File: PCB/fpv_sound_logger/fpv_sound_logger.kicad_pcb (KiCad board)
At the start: 2 copper layers, 32.1 x 25.8 mm, 47 parts, among them CN1 SM04B-SRSS-TB(LF)(SN), IC1 W25Q128JVSIQ, IC2 NCP1117ST33T3G, J1 DM3D-SF, U1 RP2040, U2 INMP441ACEZ-R7, Y1 ABM8-272-T3

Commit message: PCB: started routing
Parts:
- C1, C14, C16, C17, C18, C2, C3, D2, R4, R5, R6: moved to B.Cu
- IC2: moved to F.Cu
- moved TP1 45.7 mm to (152.8, 94.5)
- moved TP3 44.4 mm to (152.7, 96.7)
- moved TP2 42.5 mm to (150.5, 94.5)
- moved TP4 41.5 mm to (150.5, 96.7)
- moved R3 37.8 mm to (150.7, 85.9), turned to 180 degrees
- moved C16 36.4 mm to (138.8, 97.2), turned to -90 degrees
- moved R9 36.1 mm to (148.7, 96.7), turned to -90 degrees
- moved C12 35.6 mm to (151.8, 92.3)
- moved C15 35.2 mm to (149.2, 99.4)
- moved R7 35.1 mm to (147.5, 93.0)
- moved R10 33.9 mm to (146.7, 98.0)
- moved R11 33.5 mm to (146.6, 99.0)
- moved R8 33.3 mm to (148.7, 85.9), turned to 180 degrees
- moved R4 32.6 mm to (143.0, 96.4)
- moved C13 29.3 mm to (152.5, 85.5), turned to 90 degrees
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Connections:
- net Net-(U1-USB_DM) renamed /USB_DIFF-
- net Net-(U1-USB_DP) renamed /USB_DIFF+
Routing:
- net /GPIO2: track 0.00 -> 19.1 mm
- net VBUS: track 0.00 -> 19.1 mm, vias 0 -> 3
- net /GPIO1: track 0.00 -> 17.3 mm
- net /USB_D+: track 0.00 -> 12.7 mm
- net /USB_D-: track 0.00 -> 12.7 mm
- net +3V3: track 0.00 -> 10.3 mm, vias 0 -> 1
- net Net-(D1-A): track 0.00 -> 9.15 mm
- net /GPIO13: track 0.00 -> 7.87 mm, vias 0 -> 1
- net Net-(D2-K): track 0.00 -> 3.92 mm, vias 0 -> 1
- net GND: track 0.00 -> 3.85 mm
- net /USB_DIFF-: track 0.00 -> 2.15 mm
- net /USB_DIFF+: track 0.00 -> 2.15 mm
- net Net-(USB1-CC1): track 0.00 -> 1.45 mm, vias 0 -> 1
- added copper zone on F.Cu, net GND
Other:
- board size 32.1 x 25.8 mm -> 30.2 x 21.7 mm

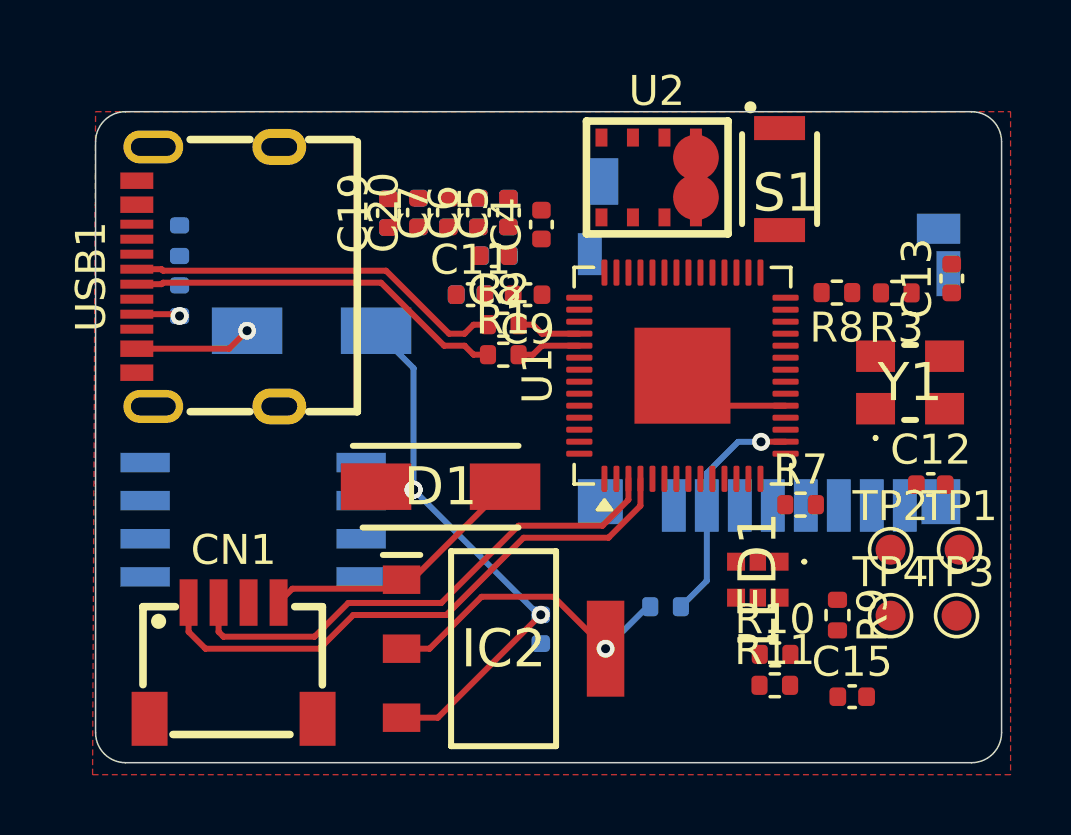
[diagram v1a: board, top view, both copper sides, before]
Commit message: PCB: finised routing - Changed clearance from 0.2 to 0.15 in the net class settings. - Increased track width from 0.3 to 0.4 for improved signal integrity. - Added a new net class for POWER with pattern GND. - Adjusted positions of GPIO labels for better alignment in the schematic:   - Moved GPIO3 from (119.38, 160.02) to (119.38, 165.1).   - Moved GPIO5 from (119.38, 165.1) to (119.38, 160.02).   - Moved GPIO10 from (129.54, 127) to (138.43, 121.92).   - Moved GPIO11 from (138.43, 121.92) to (129.54, 127).
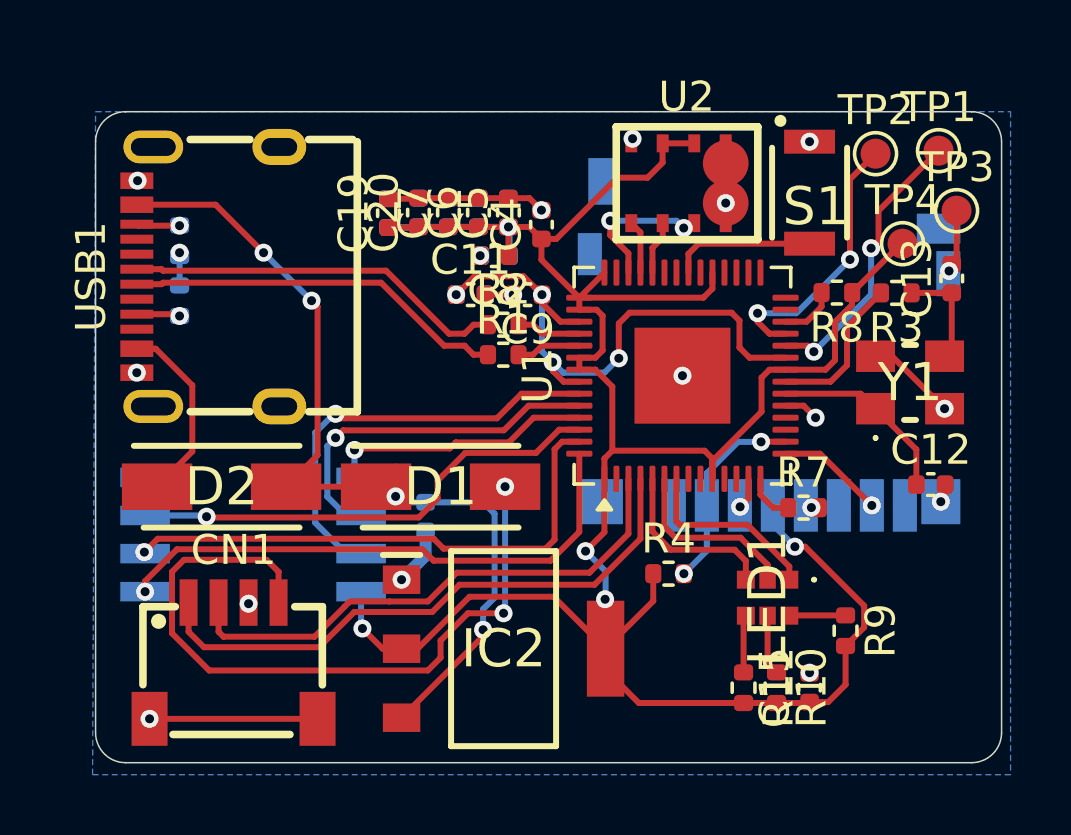
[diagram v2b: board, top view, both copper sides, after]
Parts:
- D2, R4: moved to F.Cu
- moved TP3 13.5 mm to (152.7, 83.2)
- moved TP1 13.3 mm to (152.1, 81.2)
- moved TP2 13.2 mm to (150.0, 81.3)
- moved TP4 12.4 mm to (150.9, 84.3)
- moved D2 6.00 mm to (128.2, 92.4)
- moved C16 5.37 mm to (135.0, 93.4)
- moved C15 1.45 mm to (147.8, 99.1), turned to 90 degrees
- moved R10 1.11 mm to (146.7, 99.1), turned to -90 degrees
- moved R4 1.10 mm to (143.1, 95.3)
- moved S1 1.10 mm to (147.8, 82.6)
- moved R11 1.04 mm to (145.6, 99.1), turned to -90 degrees
- moved U2 1.01 mm to (143.4, 82.3)
- moved LED1 0.68 mm to (146.4, 96.1)
- moved R9 0.59 mm to (149.0, 97.2)
- moved IC1 0.50 mm to (129.2, 94.0)
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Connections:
- J1 pad 3: /GPIO11 -> /GPIO10
- LED1 pad 1: /GPIO3 -> /GPIO5
- LED1 pad 3: /GPIO5 -> /GPIO3
- R7 pad 1: /GPIO10 -> /GPIO11
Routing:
- net +3V3: track 10.3 -> 88.2 mm, vias 1 -> 5
- net GND: track 3.85 -> 24.6 mm, vias 0 -> 18
- net +1V1: track 0.00 -> 19.6 mm, vias 0 -> 4
- net /QSPI_SS: track 0.00 -> 18.4 mm, vias 0 -> 1
- net /QSPI_SD1: track 0.00 -> 18.1 mm, vias 0 -> 1
- net /QSPI_SD2: track 0.00 -> 16.1 mm, vias 0 -> 1
- net Net-(D1-A): track 9.15 -> 23.9 mm, vias 0 -> 2
- net /QSPI_SD3: track 0.00 -> 14.4 mm, vias 0 -> 1
- net /QSPI_SCLK: track 0.00 -> 12.0 mm, vias 0 -> 1
- net VBUS: track 19.1 -> 29.7 mm, vias 3 -> 4
- net /SWCLK: track 0.00 -> 9.45 mm, vias 0 -> 2
- net /SWD: track 0.00 -> 9.09 mm, vias 0 -> 2
- net /QSPI_SD0: track 0.00 -> 9.01 mm, vias 0 -> 1
- net /XIN: track 0.00 -> 6.30 mm
- net /GPIO5: track 0.00 -> 6.25 mm
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- added copper zone on B.Cu, net GND
- removed copper zone on F.Cu, net GND

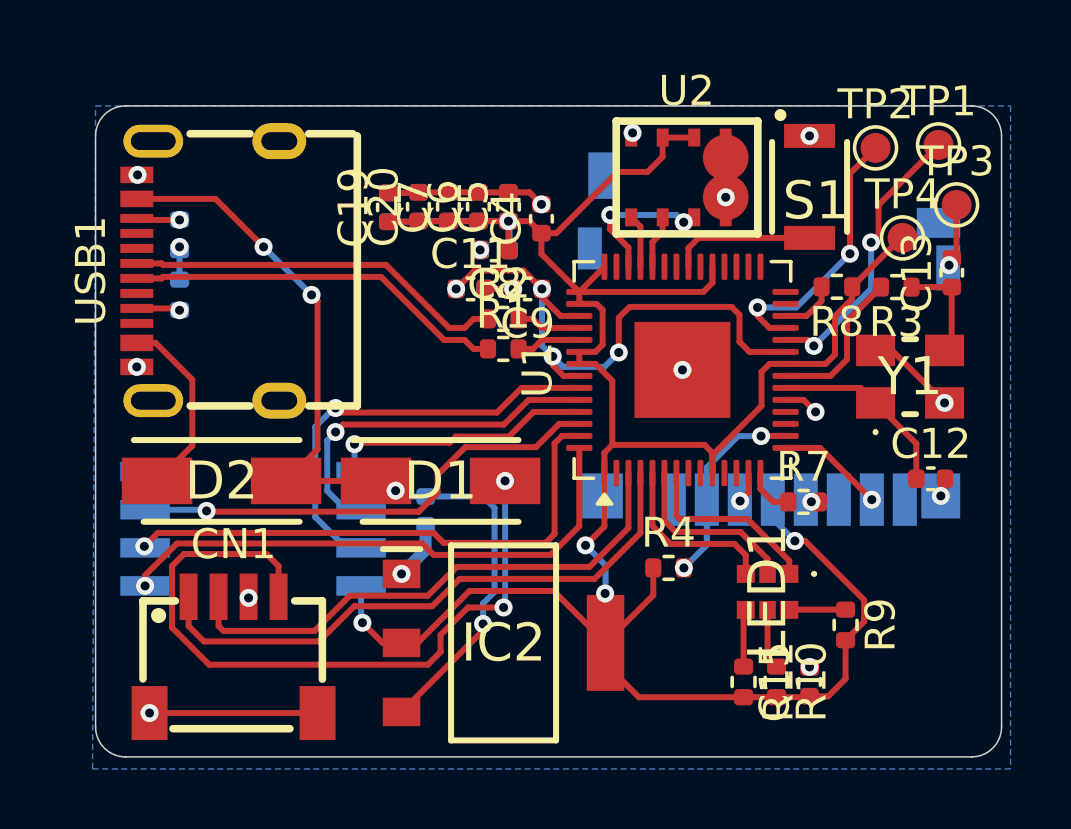
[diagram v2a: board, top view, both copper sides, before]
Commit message: PCB: finishes on board design - DRC check - Placed text - add 3d files for 3d viewer
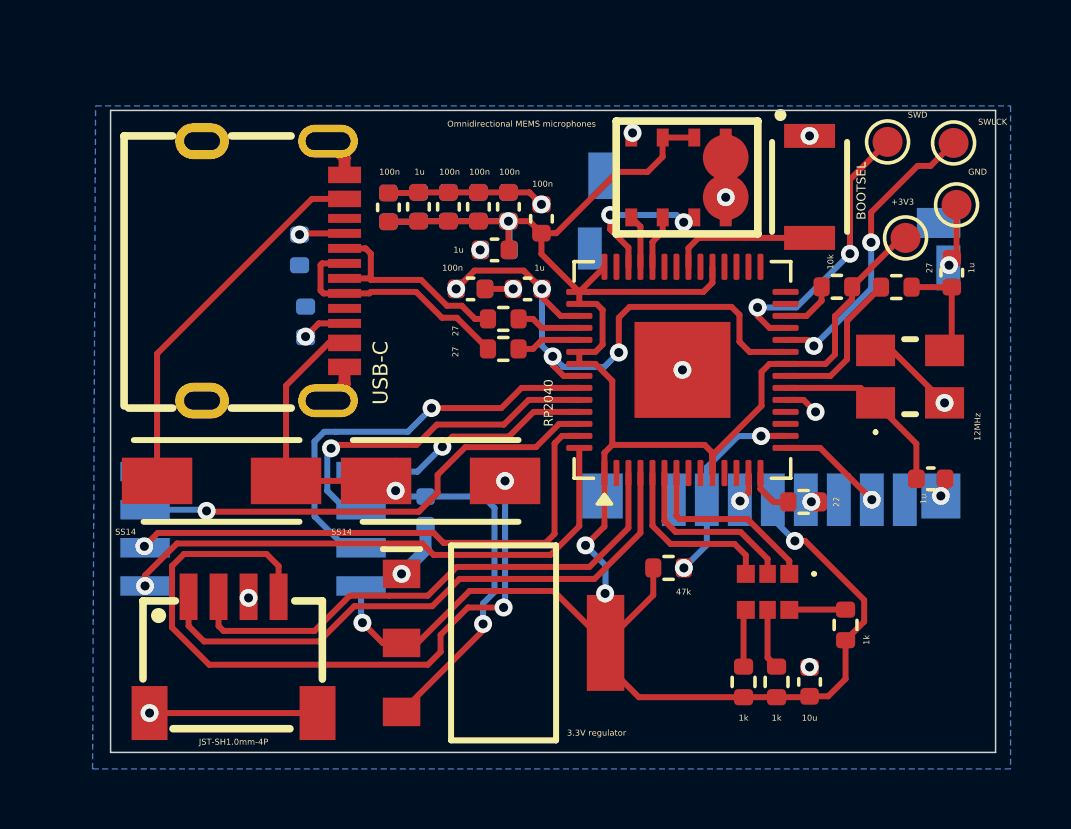
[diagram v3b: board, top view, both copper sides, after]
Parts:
- 3.3V regulator: renamed from IC2
- Flash memory: renamed from IC1
- Omnidirectional MEMS microphones: renamed from U2
- microSD card: renamed from J1
- moved 5k1 5.10 mm to (131.0, 87.1), turned to 90 degrees
- moved 5k1 4.27 mm to (130.8, 84.7), turned to -90 degrees
- moved USB-C 2.18 mm to (129.9, 85.4), turned to -90 degrees
- moved SWLCK 0.50 mm to (152.6, 81.1)
- moved SWD 0.45 mm to (150.4, 81.1)
- moved +3V3 0.10 mm to (151.0, 84.3)
- renumbered TP4 to +3V3, C19 to 100n, C1 to 100n, C18 to 100n, C7 to 100n, C11 to 100n, C6 to 100n, C5 to 100n, C4 to 100n, C3 to 100n, C10 to 100n, C2 to 100n, R8 to 10k, C15 to 10u, C16 to 10u, C17 to 10u, Y1 to 12MHz, R10 to 1k, R9 to 1k, R11 to 1k, C8 to 1u, C13 to 1u, C12 to 1u, C9 to 1u, C20 to 1u, C14 to 1u, R7 to 22, R3 to 27, R2 to 27, R1 to 27, R4 to 47k, R5 to 5k1, R6 to 5k1, TP3 to GND, CN1 to JST-SH1.0mm-4P, U1 to RP2040, D1 to SS14, D2 to SS14, TP2 to SWD, TP1 to SWLCK, USB1 to USB-C
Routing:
- net VBUS: track 29.7 -> 21.5 mm, vias 4 -> 2
- net Net-(D2-K): track 6.22 -> 12.6 mm
- net /USB_D-: track 12.7 -> 7.16 mm
- net /USB_D+: track 12.7 -> 8.10 mm
- net GND: track 24.6 -> 26.5 mm, vias 18 -> 15
- net /QSPI_SD0: track 9.01 -> 8.48 mm
- net /SWCLK: track 9.45 -> 9.97 mm
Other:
- board size 30.2 x 21.7 mm -> 29.5 x 21.4 mm
- board text added: "BOOTSEL"

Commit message: Refactor code structure and remove redundant sections for improved readability and maintainability
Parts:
- removed +3V3, GND, SWD, SWLCK: TestPoint, TestPoint:TestPoint_Pad_D1.0mm
- removed 100n (x11): 100n, Capacitor_SMD:C_0402_1005Metric
- removed 10k: 10k, Resistor_SMD:R_0402_1005Metric
- removed 10u (x3): 10u, Capacitor_SMD:C_0402_1005Metric
- removed 12MHz: ABM8-272-T3, fpv_sound_logger:ABM8272T3
- removed 1k (x3): 1k, Resistor_SMD:R_0402_1005Metric
- removed 1u (x6): 1u, Capacitor_SMD:C_0402_1005Metric
- removed 22: 22, Resistor_SMD:R_0402_1005Metric
- removed 27 (x3): 27, Resistor_SMD:R_0402_1005Metric
- removed 3.3V regulator: NCP1117ST33T3G, fpv_sound_logger:SOT230P700X180-4N
- removed 47k: 47k, Resistor_SMD:R_0402_1005Metric
- removed 5k1 (x2): 5k1, Resistor_SMD:R_0402_1005Metric
- removed Flash memory: W25Q128JVSIQ, fpv_sound_logger:SOIC127P790X216-8N
- removed JST-SH1.0mm-4P: SM04B-SRSS-TB(LF)(SN), fpv_sound_logger:CONN-SMD_4P-P1.00_SM04B-SRSS-TB-LF-SN
- removed Omnidirectional MEMS microphones: INMP441ACEZ-R7, fpv_sound_logger:MID-SMD_L4.7-W3.8_INMP441ACEZ
- removed RP2040: RP2040, Package_DFN_QFN:QFN-56-1EP_7x7mm_P0.4mm_EP3.2x3.2mm
- removed SS14 (x2): SS14, fpv_sound_logger:DIOM5227X270N
- removed USB-C: TYPE-C 16PIN 2MD(073), fpv_sound_logger:USB-C-SMD_TYPE-C-6PIN-2MD-073
- removed microSD card: DM3D-SF, fpv_sound_logger:DM3DSF
- added C1: 100n, Capacitor_SMD:C_0805_2012Metric, F.Cu at (138.0, 93.7)
- added C10: 100n, Capacitor_SMD:C_0805_2012Metric, F.Cu at (128.1, 92.4)
- added C11: 100n, Capacitor_SMD:C_0805_2012Metric, F.Cu at (128.1, 90.4)
- added C12: 15p, Capacitor_SMD:C_0805_2012Metric, F.Cu at (141.1, 84.8)
- added C13: 15p, Capacitor_SMD:C_0805_2012Metric, F.Cu at (144.4, 84.8)
- added C14: 100n, Capacitor_SMD:C_0805_2012Metric, F.Cu at (128.0, 96.4)
- added C15: 10u, Capacitor_SMD:C_0805_2012Metric, F.Cu at (161.3, 76.1)
- added C16: 10u, Capacitor_SMD:C_0805_2012Metric, F.Cu at (161.3, 79.1)
- added C17: 10u, Capacitor_SMD:C_0805_2012Metric, F.Cu at (161.3, 82.1)
- added C18: 100n, Capacitor_SMD:C_0805_2012Metric, F.Cu at (187.1, 104.0)
- added C2: 100n, Capacitor_SMD:C_0805_2012Metric, F.Cu at (135.6, 81.8)
- added C3: 100n, Capacitor_SMD:C_0805_2012Metric, F.Cu at (137.6, 81.8)
- added C4: 100n, Capacitor_SMD:C_0805_2012Metric, F.Cu at (139.6, 81.8)
- added C5: 100n, Capacitor_SMD:C_0805_2012Metric, F.Cu at (128.1, 94.4)
- added C6: 100n, Capacitor_SMD:C_0805_2012Metric, F.Cu at (141.6, 81.8)
- added C7: 100n, Capacitor_SMD:C_0805_2012Metric, F.Cu at (143.6, 81.8)
- added C8: 1u, Capacitor_SMD:C_0805_2012Metric, F.Cu at (128.1, 86.4)
- added C9: 1u, Capacitor_SMD:C_0805_2012Metric, F.Cu at (128.1, 88.4)
- added CN1: SM04B-SRSS-TB(LF)(SN), fpv_sound_logger:CONN-SMD_4P-P1.00_SM04B-SRSS-TB-LF-SN, F.Cu at (150.3, 98.3)
- added D1: MAX40203AUK+T, fpv_sound_logger:SOT95P280X145-5M, F.Cu at (151.4, 92.7)
- added D2: MAX40203AUK+T, fpv_sound_logger:SOT95P280X145-5M, F.Cu at (146.2, 92.7)
- added IC1: W25Q128JVSIQ, fpv_sound_logger:SOIC127P790X216-8N, F.Cu at (134.1, 96.7)
- added J2: MSD-4-A, fpv_sound_logger:CUI_MSD-4-A, B.Cu at (133.2, 94.3)
- added LED2: LTST-C171KRKT, fpv_sound_logger:LED_LTST-C171_LTO-M, F.Cu at (145.0, 97.9)
- added R1: 27.4, Capacitor_SMD:C_0805_2012Metric, F.Cu at (139.1, 85.7)
- added R10: 1k, Capacitor_SMD:C_0805_2012Metric, F.Cu at (187.1, 110.0)
- added R11: 1k, Capacitor_SMD:C_0805_2012Metric, F.Cu at (187.1, 113.1)
- added R12: 10k, Capacitor_SMD:C_0805_2012Metric, F.Cu at (170.2, 113.1)
- added R13: 1k, Capacitor_SMD:C_0805_2012Metric, F.Cu at (144.9, 95.7)
- added R2: 27.4, Capacitor_SMD:C_0805_2012Metric, F.Cu at (139.1, 88.7)
- added R3: 1k, Capacitor_SMD:C_0805_2012Metric, F.Cu at (170.2, 110.0)
- added R5: 5k1, Capacitor_SMD:C_0805_2012Metric, F.Cu at (161.3, 91.2)
- added R6: 5k1, Capacitor_SMD:C_0805_2012Metric, F.Cu at (161.3, 94.2)
- added R9: 1k, Capacitor_SMD:C_0805_2012Metric, F.Cu at (187.1, 107.0)
- added TP1: TestPoint, TestPoint:TestPoint_Pad_D1.0mm, F.Cu at (180.9, 76.1)
- added TP2: TestPoint, TestPoint:TestPoint_Pad_D1.0mm, F.Cu at (180.9, 79.2)
- added TP3: TestPoint, TestPoint:TestPoint_Pad_D1.0mm, F.Cu at (180.9, 82.2)
- added TP4: TestPoint, TestPoint:TestPoint_Pad_D1.0mm, F.Cu at (180.9, 85.3)
- added U2: INMP441ACEZ-R7, fpv_sound_logger:MID-SMD_L4.7-W3.8_INMP441ACEZ, F.Cu at (126.7, 83.0)
- added U3: TLV75533PDBVR, fpv_sound_logger:SOT95P280X145-5N, F.Cu at (141.5, 92.7)
- added U4: SC0914_13_, fpv_sound_logger:QFN40P700X700X90-57N, F.Cu at (133.9, 87.9)
- added USB1: TYPE-C 16PIN 2MD(073), fpv_sound_logger:USB-C-SMD_TYPE-C-6PIN-2MD-073, F.Cu at (150.4, 85.4)
- added Y1: ABM8-272-T3, fpv_sound_logger:ABM8272T3, F.Cu at (141.1, 92.6)
- moved LED1 20.1 mm to (126.6, 99.5)
- moved S1 16.3 mm to (131.5, 81.4), turned to 180 degrees
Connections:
- LED1 pad 1: /GPIO5 -> GPIO2
- LED1 pad 2: /GPIO4 -> GPIO4
- LED1 pad 3: /GPIO3 -> GPIO3
- LED1 pad 4: Net-(LED1-A_BLUE) -> /sensor/BLUE
- LED1 pad 5: Net-(LED1-A_RED) -> /sensor/RED
- LED1 pad 6: Net-(LED1-A_GREEN) -> /sensor/GREEN
- S1 pad 2: /GPIO23 -> GPIO23
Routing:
- net +3V3: track 88.3 -> 0.00 mm, vias 5 -> 0
- net GND: track 26.5 -> 0.00 mm, vias 15 -> 0
- net Net-(D1-A): track 23.9 -> 0.00 mm, vias 2 -> 0
- net VBUS: track 21.5 -> 0.00 mm, vias 2 -> 0
- net /GPIO2: track 19.7 -> 0.00 mm
- net +1V1: track 19.6 -> 0.00 mm, vias 4 -> 0
- net /QSPI_SS: track 18.4 -> 0.00 mm, vias 1 -> 0
- net /QSPI_SD1: track 18.1 -> 0.00 mm, vias 1 -> 0
- net /GPIO1: track 18.0 -> 0.00 mm
- net /QSPI_SD2: track 16.1 -> 0.00 mm, vias 1 -> 0
- net /QSPI_SD3: track 14.0 -> 0.00 mm, vias 1 -> 0
- net Net-(D2-K): track 12.6 -> 0.00 mm
- net /QSPI_SCLK: track 11.8 -> 0.00 mm, vias 1 -> 0
- net /SWCLK: track 9.97 -> 0.00 mm, vias 2 -> 0
- net /SWD: track 9.45 -> 0.00 mm, vias 2 -> 0
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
